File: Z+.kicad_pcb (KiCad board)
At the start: 4 copper layers, 98 x 98 mm, 225 parts, among them J1 200528-0100, J2 Conn_01x04_MountingPin, J3 USB4110GFA, J4 BG301-06-X-XXXX-X-X_REVC, J5 BG301-06-X-XXXX-X-X_REVC, Q1 NX3008NBKS, Q10 NX3008NBKS, Q11 MBT2222ADW1T1, Q12 NX3008NBKS, Q13 MBT2222ADW1T1, Q14 NX3008NBKS, Q15 MBT2222ADW1T1, Q16 NX3008NBKS, Q17 MBT2222ADW1T1, Q18 NX3008NBKS, Q19 MBT2222ADW1T1, Q2 MBT2222ADW1T1, Q20 NX3008NBKS, Q21 MBT2222ADW1T1, Q22 NX3008NBKS, Q23 MBT2222ADW1T1, Q24 NX3008NBKS, Q25 MBT2222ADW1T1, Q26 NX3008NBKS, Q27 MBT2222ADW1T1, Q3 NX3008NBKS, Q4 MBT2222ADW1T1, Q5 NX3008NBKS, Q6 MBT2222ADW1T1, Q7 SiRA99DP, Q8 IRLML2803, Q9 SiRA99DP, U1 USBLC6-2P6, U10 USBLC6-2P6, U2 SunSensor, U3 SunSensor, U4 SunSensor, U5 SunSensor, U6 LTC4412xS6, U7 DRV8235RTER, U8 ADM1176-1ARMZ-R7, U9 LTC3130

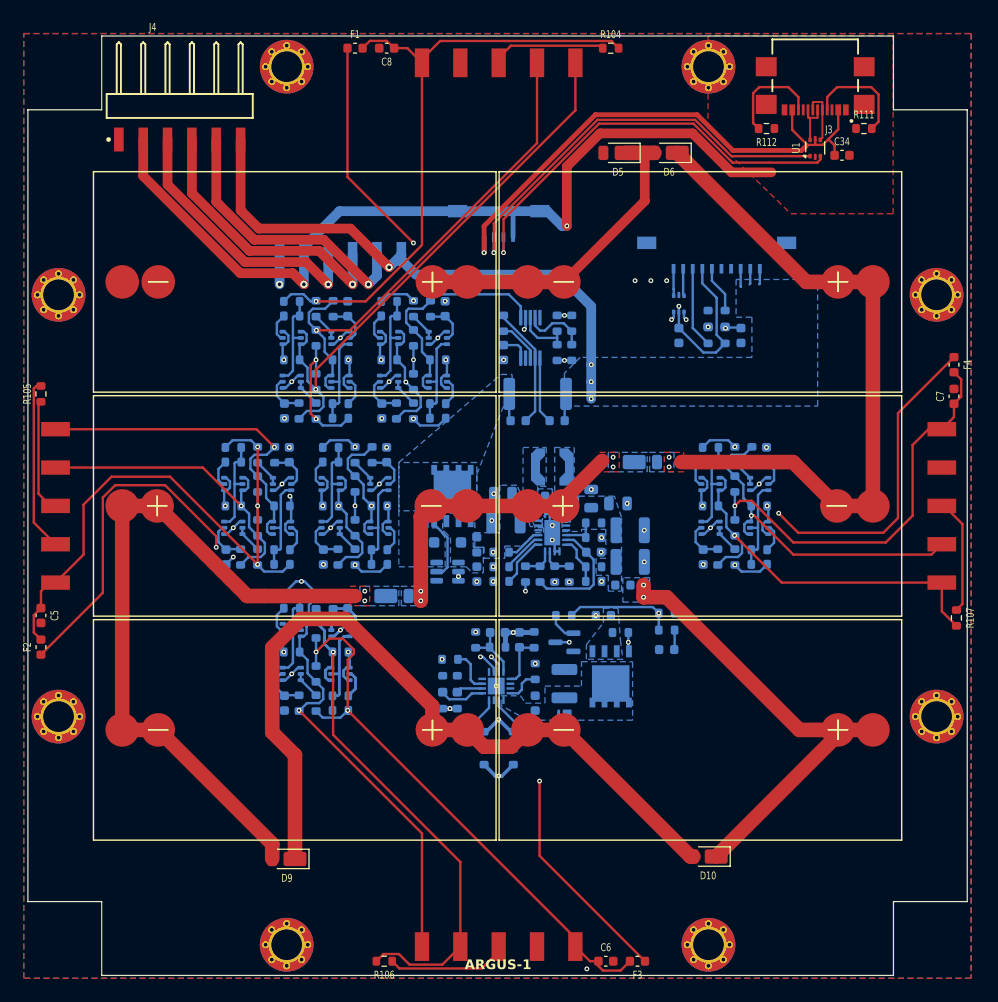
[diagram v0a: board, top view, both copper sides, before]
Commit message: Cleaned up silkscreen
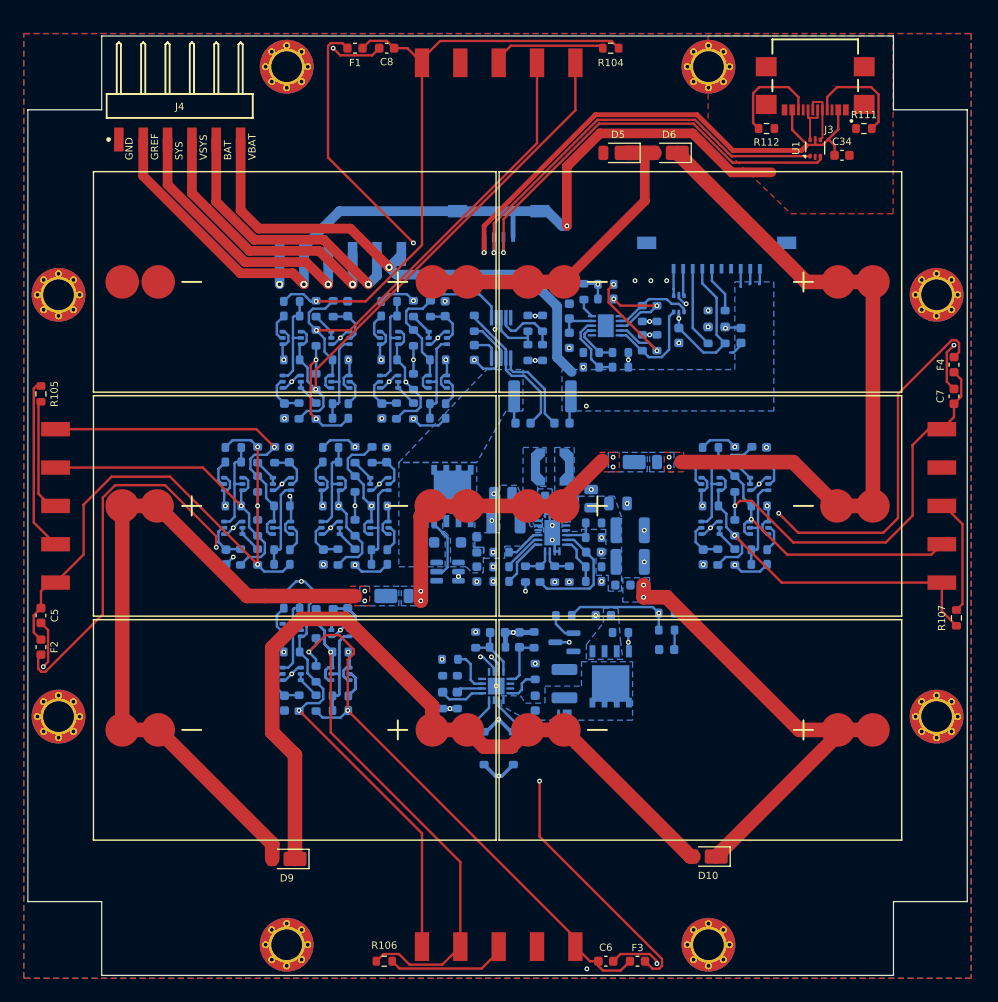
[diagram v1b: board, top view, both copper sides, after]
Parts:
- added C35: 0.1uF, Capacitor_SMD:C_0603_1608Metric, B.Cu at (157.7, 81.5)
- added F10: 100mA, Fuse:Fuse_0603_1608Metric, B.Cu at (157.7, 84.6)
- added R117: ?, Resistor_SMD:R_0603_1608Metric, B.Cu at (163.1, 87.4)
- added R118: ?, Resistor_SMD:R_0603_1608Metric, B.Cu at (160.0, 87.4)
- added R119: ?, Resistor_SMD:R_0603_1608Metric, B.Cu at (163.1, 85.9)
- added R120: ?, Resistor_SMD:R_0603_1608Metric, B.Cu at (160.0, 85.9)
- added R121: 10K, Resistor_SMD:R_0603_1608Metric, B.Cu at (159.3, 79.5)
- added R122: 10K, Resistor_SMD:R_0603_1608Metric, B.Cu at (161.5, 80.3)
- added R123: 10K, Resistor_SMD:R_0603_1608Metric, B.Cu at (161.5, 78.7)
- added R124: 0R, Resistor_SMD:R_0603_1608Metric, B.Cu at (166.9, 84.8)
- added R125: 0R, Resistor_SMD:R_0603_1608Metric, B.Cu at (166.9, 81.8)
- added R126: 0R (DNI), Resistor_SMD:R_0603_1608Metric, B.Cu at (165.4, 84.8)
- added R127: 0R (DNI), Resistor_SMD:R_0603_1608Metric, B.Cu at (165.4, 81.8)
- added U11: LTC4316xDD, Package_DFN_QFN:DFN-10-1EP_3x3mm_P0.5mm_EP1.65x2.38mm, B.Cu at (161.5, 83.1)
- SC1, SC2, SC3, SC4, SC5, SC6: value SM141K06TF -> SM141K06L
- moved C17 3.05 mm to (147.8, 85.9)
- moved R108 3.05 mm to (153.4, 85.9)
- moved R109 3.05 mm to (154.9, 82.8)
- moved R110 3.05 mm to (154.9, 85.9)
- moved R56 3.05 mm to (147.8, 82.8)
- moved R57 3.05 mm to (153.4, 82.8)
- moved U8 3.05 mm to (150.6, 84.3)
- moved F8 0.57 mm to (157.0, 93.2)
- moved R55 0.57 mm to (154.9, 90.4)
- moved F9 0.57 mm to (152.9, 93.2)
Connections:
- net /Interfaces/BATT renamed /Interfaces/RBF/BATT
- net /Interfaces/CC1 renamed /Interfaces/USB-C/CC1
- net /Interfaces/CC2 renamed /Interfaces/USB-C/CC2
- net /Interfaces/COIL_DRIVER_EN_OR_MAIN_3V3 renamed /Interfaces/Mainboard FPC/COIL_DRIVER_EN_OR_MAIN_3V3
- net /Interfaces/D+ renamed /Interfaces/USB-C/D+
- net /Interfaces/D- renamed /Interfaces/USB-C/D-
- net /Interfaces/D_CONN+ renamed /Interfaces/USB-C/D_CONN+
- net /Interfaces/D_CONN- renamed /Interfaces/USB-C/D_CONN-
- net /Interfaces/PERI_3V3_OR_GND renamed /Interfaces/Mainboard FPC/PERI_3V3_OR_GND
- net /Interfaces/SYS renamed /Interfaces/RBF/SYS
- net /Interfaces/VSYS renamed /Interfaces/RBF/VSYS
- R33 pad 2: PERI_3V3 -> MAIN_3V3
- U10 pad 4: SDA -> SDA_MB
- U10 pad 6: SCL -> SCL_MB
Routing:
- net PERI_3V3: track 335.5 -> 364.4 mm, vias 6 -> 8
- net GND: track 68.9 -> 96.8 mm, vias 46 -> 54
- net /I2C Translator/SCLOUT: track 0.00 -> 14.0 mm, vias 0 -> 2
- net MAIN_3V3: track 42.1 -> 52.9 mm, vias 11 -> 12
- net SCL_MB: track 0.00 -> 10.5 mm
- net SCL: track 136.0 -> 146.3 mm
- net VBATT: track 94.8 -> 85.1 mm, vias 5 -> 3
- net /I2C Translator/SDAOUT: track 0.00 -> 9.55 mm, vias 0 -> 2
- net SDA_MB: track 0.00 -> 8.38 mm
- net Net-(U11-XORL): track 0.00 -> 7.29 mm
- net Net-(U11-XORH): track 0.00 -> 4.89 mm
- net Net-(U11-V_{CC}): track 0.00 -> 3.95 mm
- net SCL_SPWR: track 24.3 -> 21.3 mm
- net SDA_SPWR: track 28.7 -> 25.7 mm
- net Net-(U8-VCC): track 6.94 -> 9.54 mm
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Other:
- board text added: "5V"
- board text added: "ARGUS-1 Cubesat Carnegie Mellon University Z+ Solar Panel v2"
- board text added: "BAT"
- board text added: "CDEN"
- board text added: "D+"
- board text added: "D-"
- board text added: "GREF"
- board text added: "M3V3"
- board text added: "P3V3"
- board text added: "SYS"
- board text added: "VBAT"
- board text added: "VSYS"
- board text removed: "3.3V"
- board text removed: "ARGUS-1"
- board text removed: "ARGUS-1 Cubesat Carnegie Mellon University Z+ Solar Panel v1"
- board text removed: "Charge Sense"
- board text removed: "Coil Power Sense"
- board text removed: "I2C BUS PROTECTION"
- board text removed: "MPPT"
- board text removed: "OR-ing"
- board text removed: "SCL CHARGE SENSE"
- board text removed: "SCL COIL DRIVER"
- board text removed: "SCL COIL SENSE"
- board text removed: "SCL LS"
- board text removed: "SDA CHARGE SENSE"
- board text removed: "SDA COIL DRIVER"
- board text removed: "SDA COIL SENSE"
- board text removed: "SDA LS"
- board text removed: "VSOLAR"
